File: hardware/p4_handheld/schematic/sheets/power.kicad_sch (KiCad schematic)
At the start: 13 parts, among them J1 HRO-TYPE-C-31-M-12, J2 1S-Protected-LiPo, SW9 SlideSwitch-SPDT-JS102000-cla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, U2 BQ24075RGTR, U3 MAX17048G+T10, U4 TPS63070, U6 TPS22919DCK

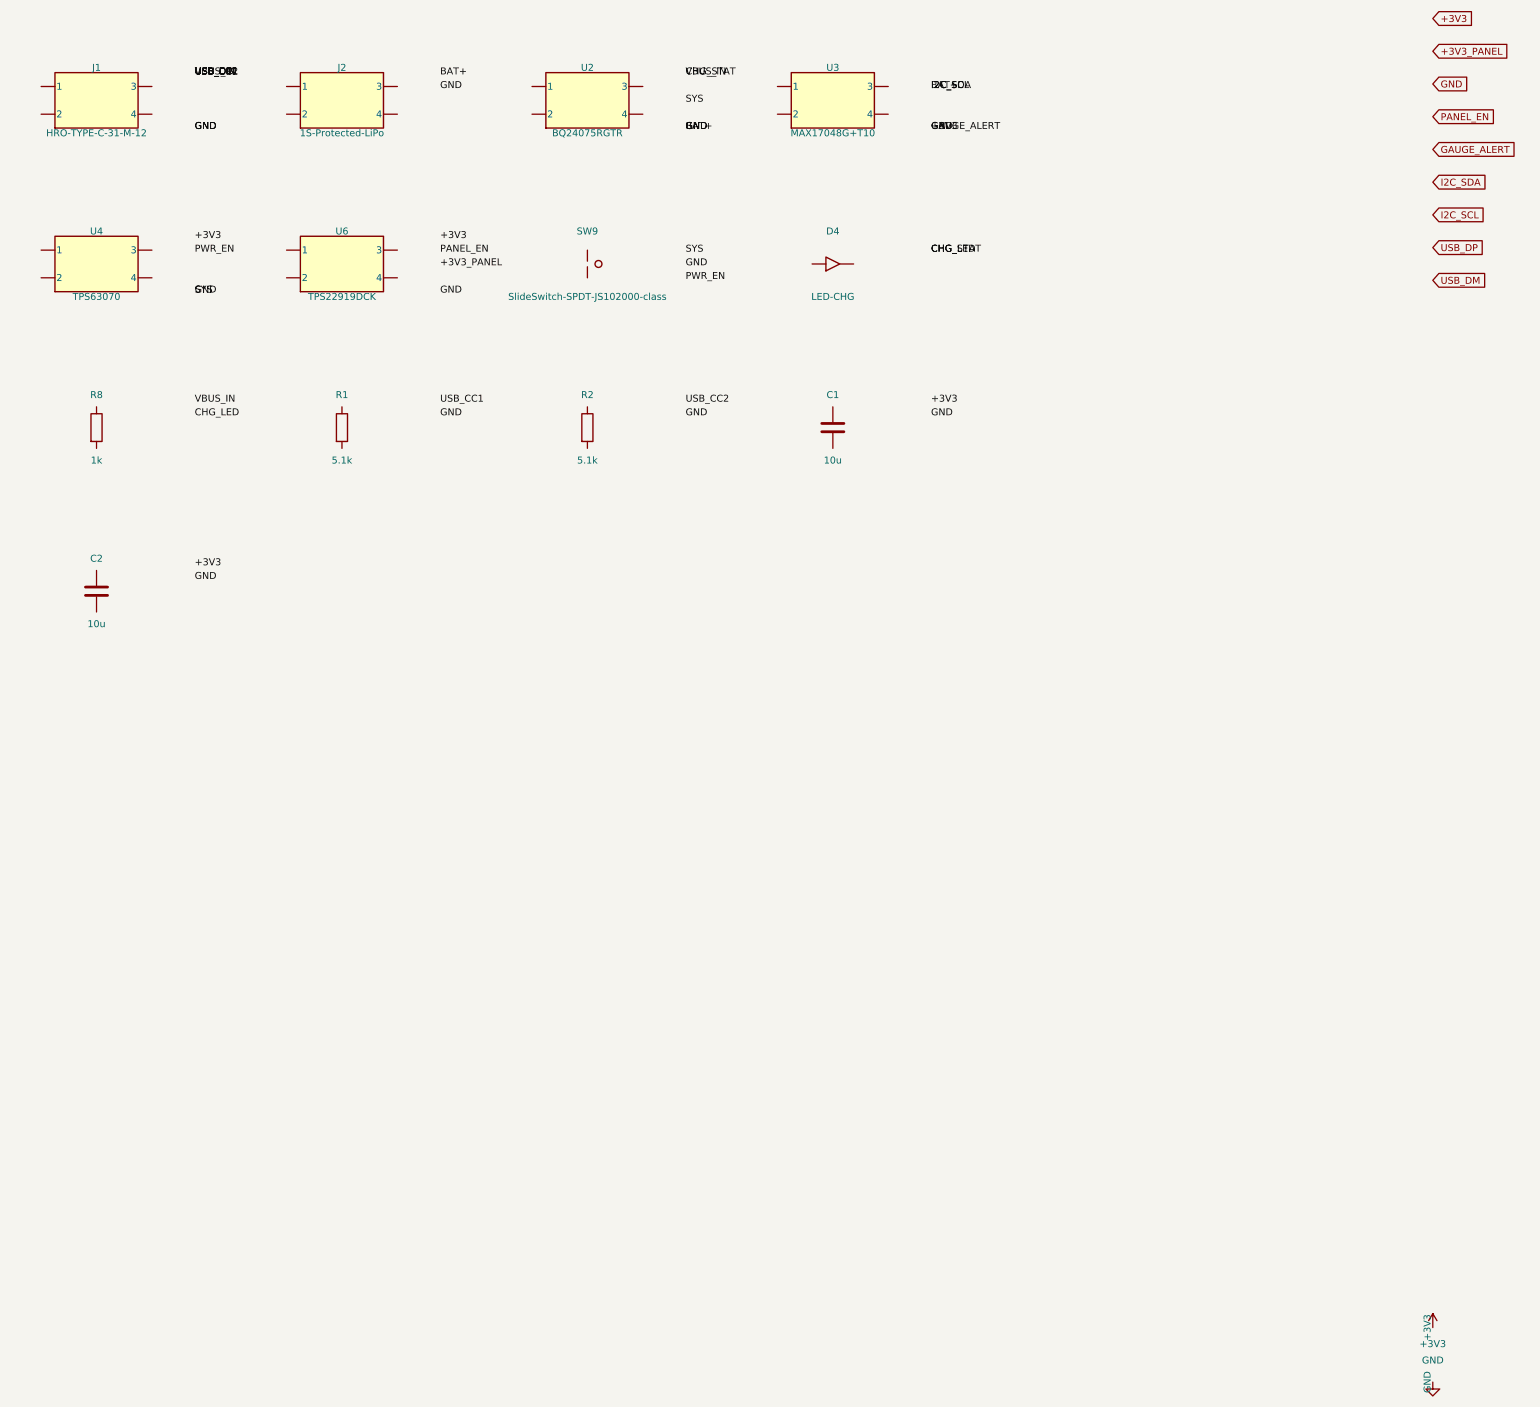
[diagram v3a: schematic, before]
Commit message: hw(p4_handheld): ERC-clean schematic engine (real pins, on-endpoint labels, project symbol lib)
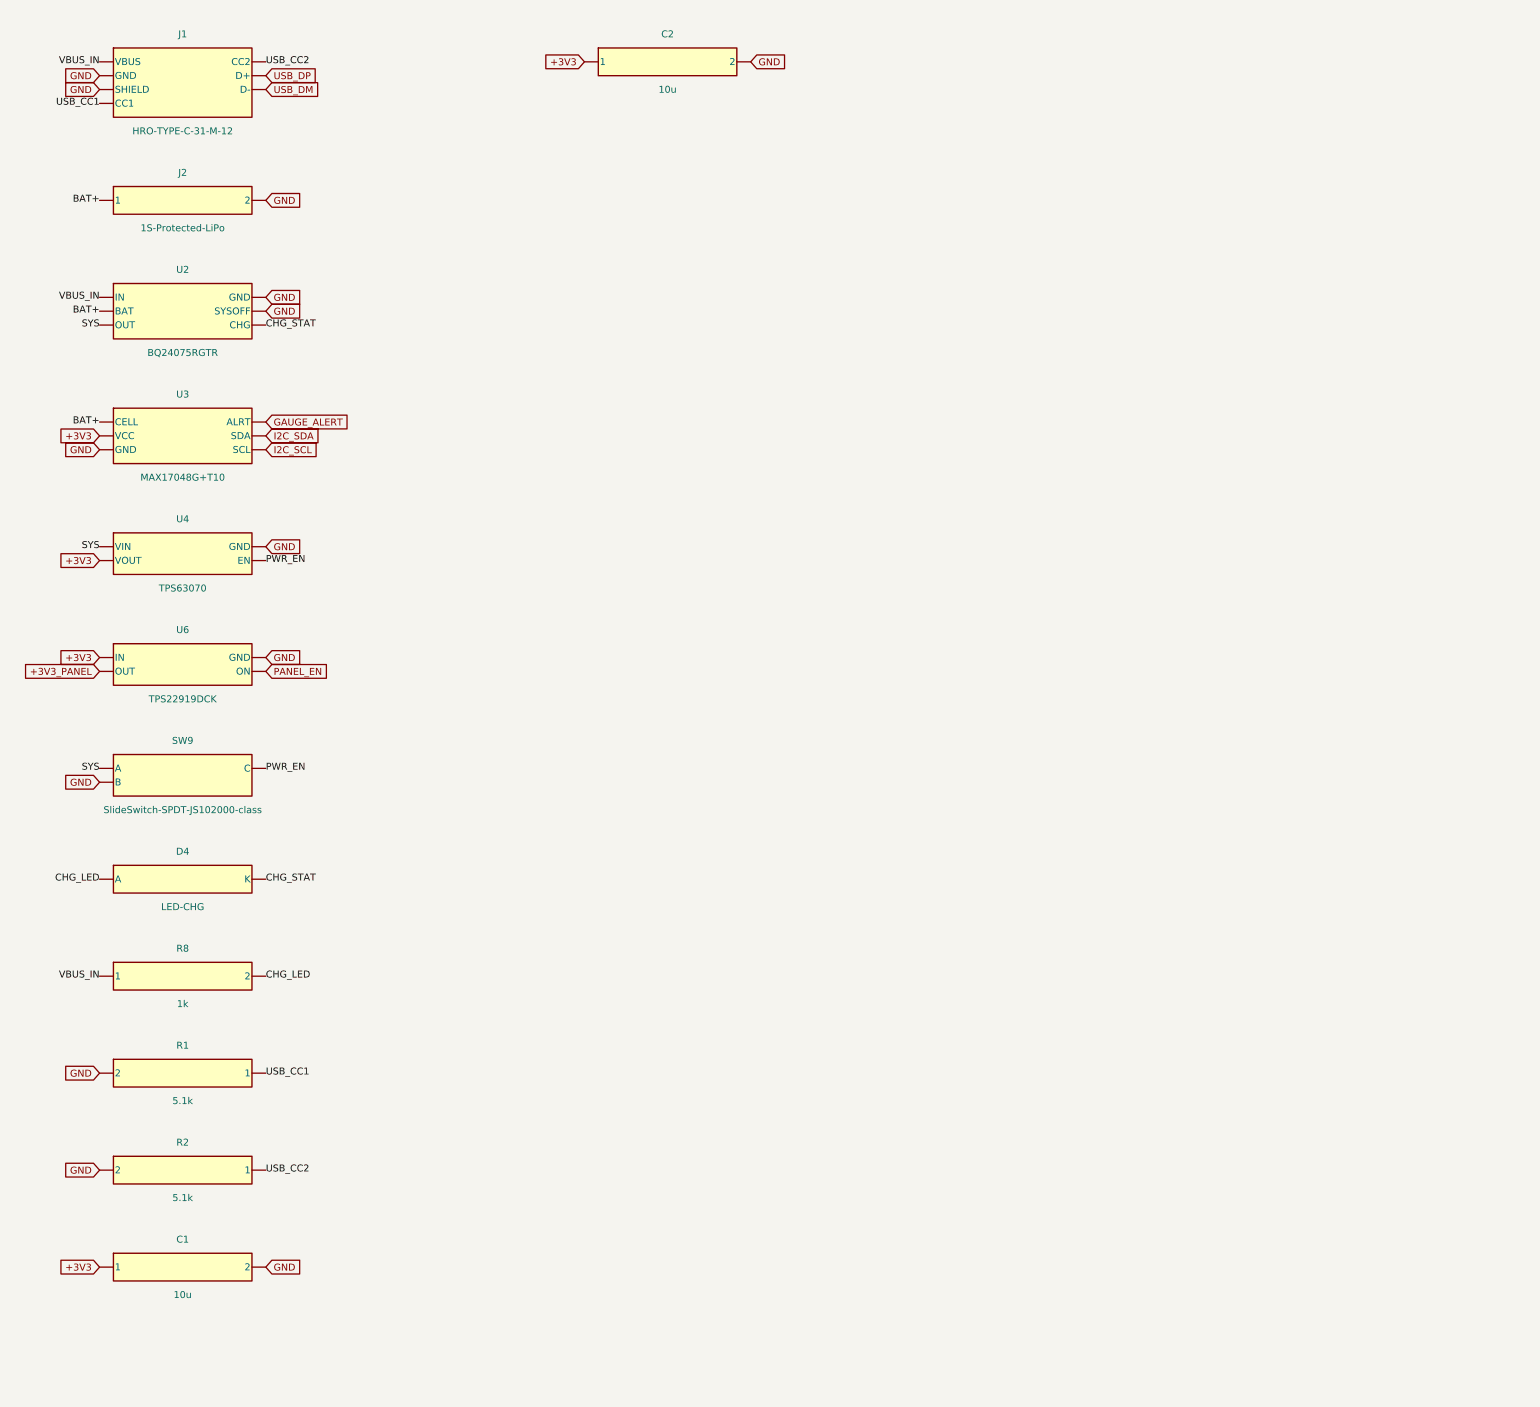
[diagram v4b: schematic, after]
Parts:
- removed C1: 10u, C0603, symbol Device:C
- removed D4: LED-CHG, LED0603-RD, symbol Device:LED
- removed J1: HRO-TYPE-C-31-M-12, USB-C-SMD_TYPE-C-16PIN-2MD-073, symbol PSP4H:Block2
- removed J2: 1S-Protected-LiPo, CONN-SMD_SM02B-SRSS-TB, symbol PSP4H:Block2
- removed R2: 5.1k, R0402, symbol Device:R
- removed R8: 1k, R0402, symbol Device:R
- removed SW9: SlideSwitch-SPDT-JS102000-class, SW-SMD_6P-L7.0-W3.5-P1.27-LS4.5-TL, symbol Switch:SW_Push
- removed U2: BQ24075RGTR, QFN-16_L3.0-W3.0-P0.50-TL-EP1.7, symbol PSP4H:Block2
- removed U3: MAX17048G+T10, TDFN-8_L2.0-W2.0-P0.50-BL-EP1.2, symbol PSP4H:Block2
- removed U4: TPS63070, VQFN-HR-15_L3.0-W2.5-P0.50-BL_TPS63070RNMR, symbol PSP4H:Block2
- removed U6: TPS22919DCK, SC-70-6_L2.2-W1.3-P0.65-LS2.1-BR, symbol PSP4H:Block2
- added C1: 10u, symbol PSP4H:SYM_C1
- added C2: 10u, symbol PSP4H:SYM_C2
- added D4: LED-CHG, symbol PSP4H:SYM_D4
- added J1: HRO-TYPE-C-31-M-12, symbol PSP4H:SYM_J1
- added J2: 1S-Protected-LiPo, symbol PSP4H:SYM_J2
- added R1: 5.1k, symbol PSP4H:SYM_R1
- added R2: 5.1k, symbol PSP4H:SYM_R2
- added R8: 1k, symbol PSP4H:SYM_R8
- added SW9: SlideSwitch-SPDT-JS102000-class, symbol PSP4H:SYM_SW9
- added U2: BQ24075RGTR, symbol PSP4H:SYM_U2
- added U3: MAX17048G+T10, symbol PSP4H:SYM_U3
- U4: renamed from R1; value 5.1k -> TPS63070; footprint R0402 -> (none); symbol Device:R -> PSP4H:SYM_U4; FootprintPlan (none) -> VQFN-HR-15_L3.0-W2.5-P0.50-BL_TPS63070RNMR; LCSC C25905 -> C964639; MPN 0402WGF5101TCE -> TPS63070RNMT
- U6: renamed from C2; value 10u -> TPS22919DCK; footprint C0603 -> (none); symbol Device:C -> PSP4H:SYM_U6; FootprintPlan (none) -> SC-70-6_L2.2-W1.3-P0.65-LS2.1-BR; LCSC C19702 -> C2149796; MPN CL10A106KP8NNNC -> TPS22919DCKR
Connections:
- net +3V3_PANEL: now also U6.OUT
- net GND: now also U4.GND, U6.GND, C1.2, C2.2, J1.GND, J1.SHIELD, J2.2, R1.2, R2.2, SW9.B, U2.GND, U2.SYSOFF, U3.GND
- net PANEL_EN: now also U6.ON
- net PWR_EN: now also U4.EN, SW9.C
- net USB_DM: now also J1.D-
- new net +3V3: C1.1, C2.1, U3.VCC, U4.VOUT, U6.IN
- new net BAT+: J2.1, U2.BAT, U3.CELL
- new net CHG_LED: D4.A, R8.2
- new net CHG_STAT: D4.K, U2.CHG
- new net GAUGE_ALERT: U3.ALRT
- new net I2C_SCL: U3.SCL
- new net I2C_SDA: U3.SDA
- new net SYS: SW9.A, U2.OUT, U4.VIN
- new net USB_CC1: J1.CC1, R1.1
- new net USB_CC2: J1.CC2, R2.1
- new net USB_DP: J1.D+
- new net VBUS_IN: J1.VBUS, R8.1, U2.IN
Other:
- title: PuzzleScript Card — power -> PuzzleScript P4 Handheld — power
